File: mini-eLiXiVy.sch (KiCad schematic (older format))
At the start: 175 parts, among them J1 TYPE-C-31-M12_13_EDITED, J2 AVR-ISP-6, SW1 SW_Push, U1 ATmega32U4-AU, U2 WE-TVS-82400102, Y1 Crystal_GND24_Small

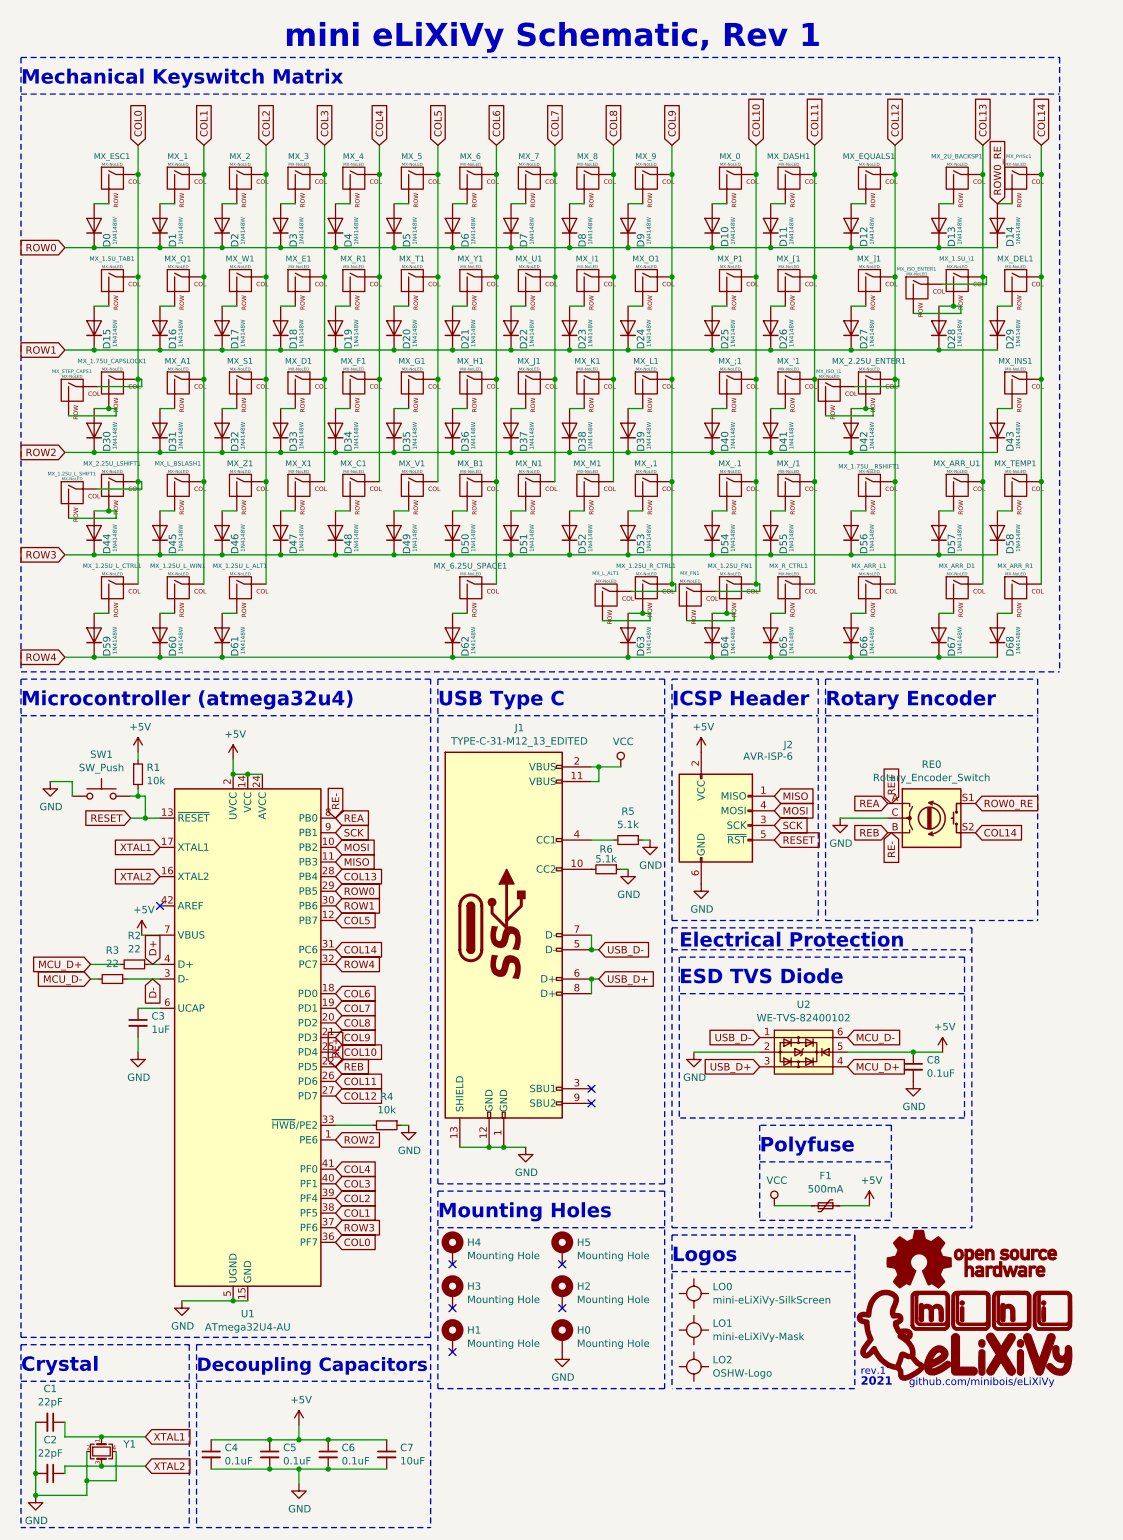
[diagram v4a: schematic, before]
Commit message: Updated logo, refined data line traces.
Logos have been updated to match the revision number, rev.1.1
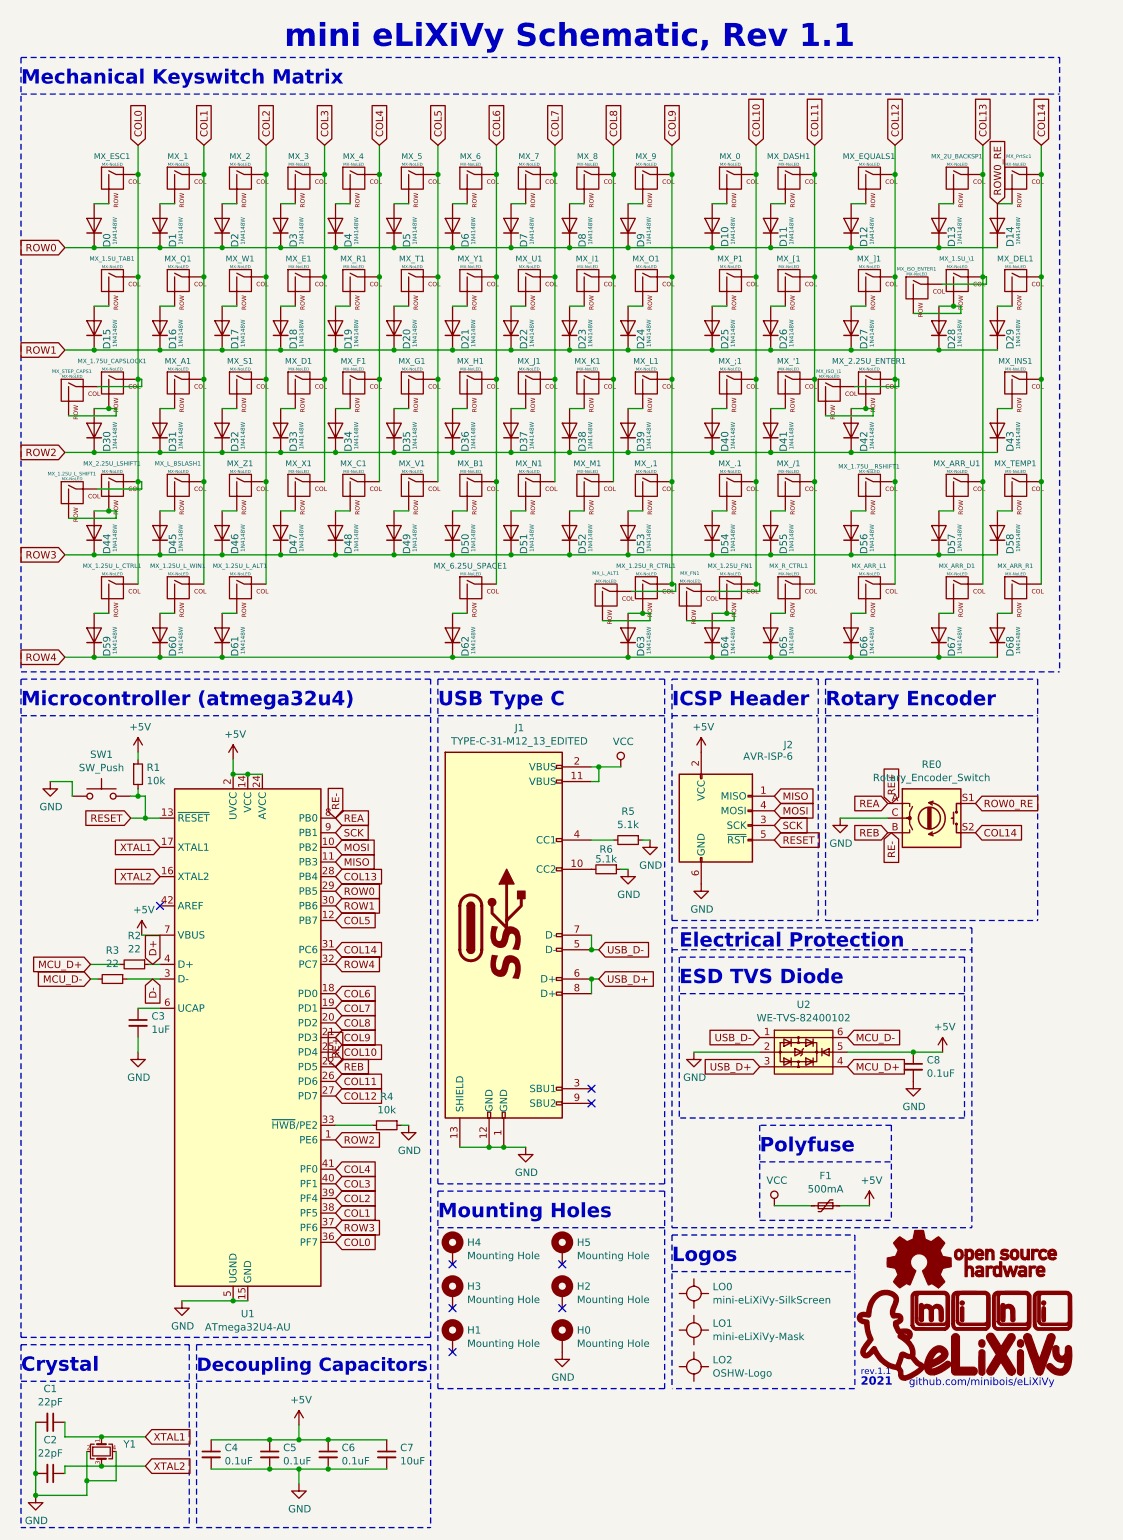
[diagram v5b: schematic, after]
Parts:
- LO0: footprint mini-Logos:eLiXiVy-SilkScreenv2 -> mini-Logos:eLiXiVy-rev1.1-SilkScreen
- LO1: footprint mini-Logos:eLiXiVy-Maskv2 -> mini-Logos:eLiXiVy-rev1.1-Mask
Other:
- note added: "mini eLiXiVy Schematic, Rev 1.1"
- note added: "rev.1.1"
- note removed: "mini eLiXiVy Schematic, Rev 1"
- note removed: "rev.1"
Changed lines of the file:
@@
 Sheet 1 1
 Title "eLiXiVy"
-Date "2021-08-05"
-Rev "1"
+Date "2021-08-23"
+Rev "1.1"
 Comp "Full License: https://github.com/minibois/eLiXiVy/blob/master/LICENSE.txt"
 Comment1 "of CERN_OHL-S v2 (https://ohwr.org/cern_ohl_s_v2.txt)"
@@
 COL13
 Text Notes 2400 750  0    157  ~ 31
-mini eLiXiVy Schematic, Rev 1
+mini eLiXiVy Schematic, Rev 1.1
 $Comp
 L power:GND #PWR0109
@@
 F 0 "LO0" H 5328 8796 50  0000 L CNN
 F 1 "mini-eLiXiVy-SilkScreen" H 5328 8705 50  0000 L CNN
-F 2 "mini-Logos:eLiXiVy-SilkScreenv2" H 5200 8900 50  0001 C CNN
+F 2 "mini-Logos:eLiXiVy-rev1.1-SilkScreen" H 5200 8900 50  0001 C CNN
 F 3 "" H 5200 8900 50  0001 C CNN
 	1    5200 9000
@@
 F 0 "LO1" H 5328 9046 50  0000 L CNN
 F 1 "mini-eLiXiVy-Mask" H 5328 8955 50  0000 L CNN
-F 2 "mini-Logos:eLiXiVy-Maskv2" H 5200 9150 50  0001 C CNN
+F 2 "mini-Logos:eLiXiVy-rev1.1-Mask" H 5200 9150 50  0001 C CNN
 F 3 "" H 5200 9150 50  0001 C CNN
 	1    5200 9250
@@
 	1    0    0    -1
 $EndComp
-Text Notes 6340 9815 0    49   ~ 0
-rev.1
+Text Notes 6340 9815 0    43   ~ 0
+rev.1.1
 Text Notes 6340 9890 0    57   ~ 11
 2021
